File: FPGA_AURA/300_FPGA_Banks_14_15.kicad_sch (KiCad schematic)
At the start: 1 part, among them U1 XC7A35T-2FTG256C

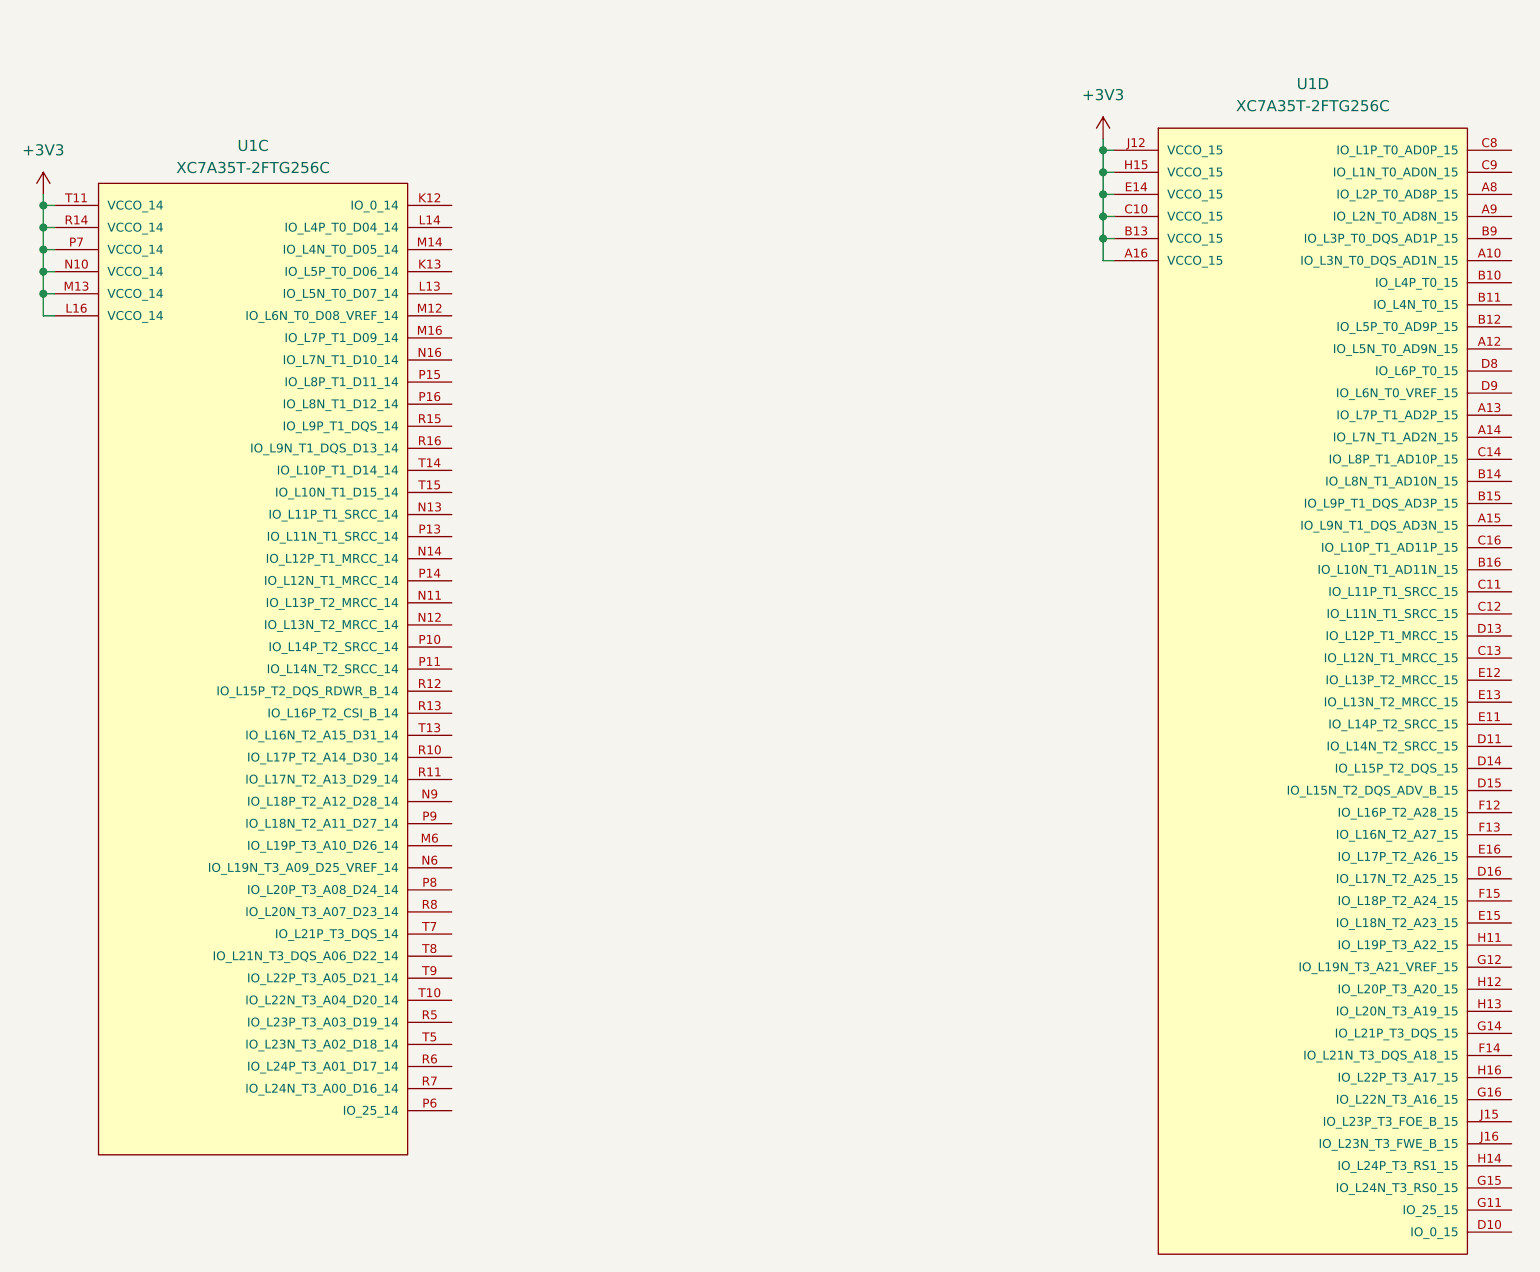
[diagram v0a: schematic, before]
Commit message: Added USB power schottky and started DDR3L
Transferring from laptop to PC to decide DDR3 pins.
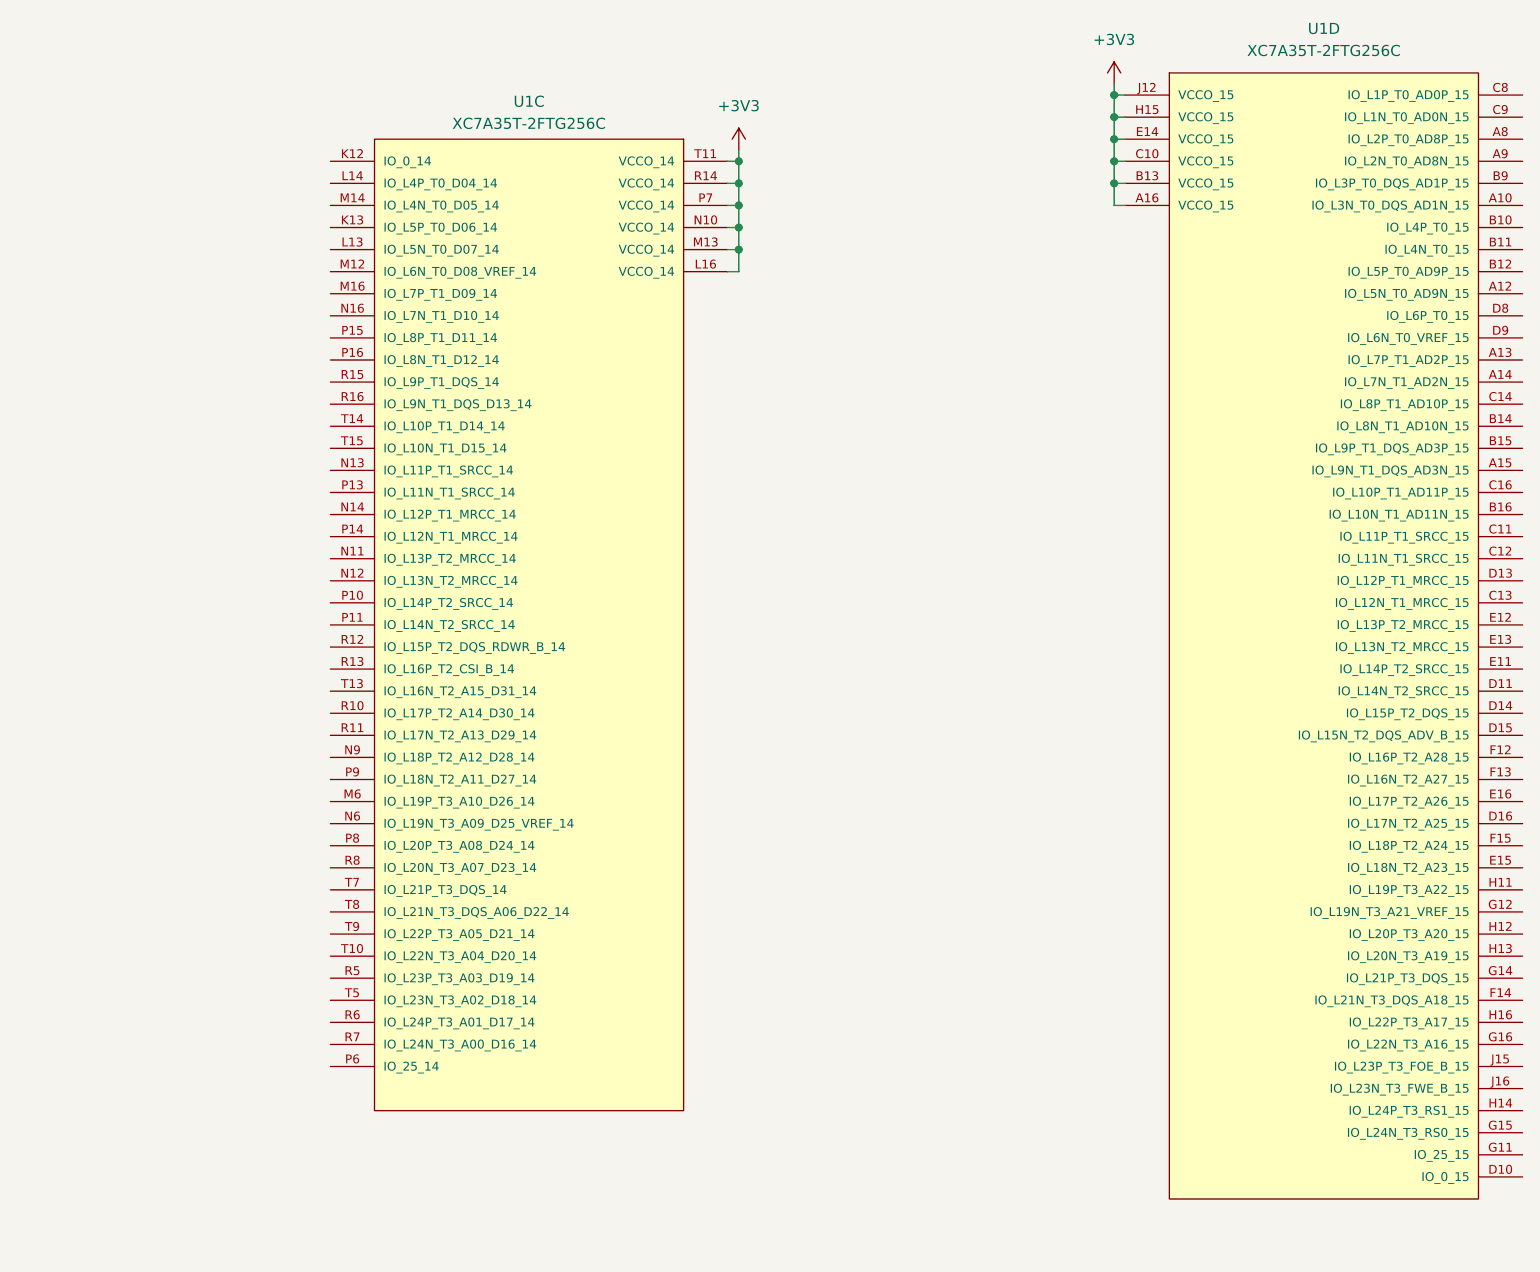
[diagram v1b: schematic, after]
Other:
- moved on the sheet: U1C, U1D

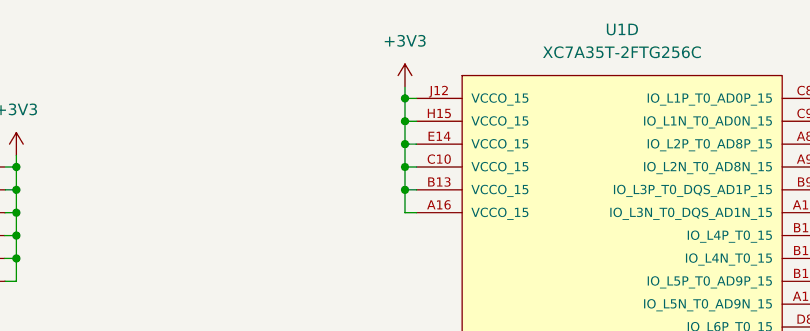
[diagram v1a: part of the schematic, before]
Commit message: Moving to PC.
Placed the VTT termination resistors roughly, rotated the DDR IC 180, and deleted the initial draft of routing.
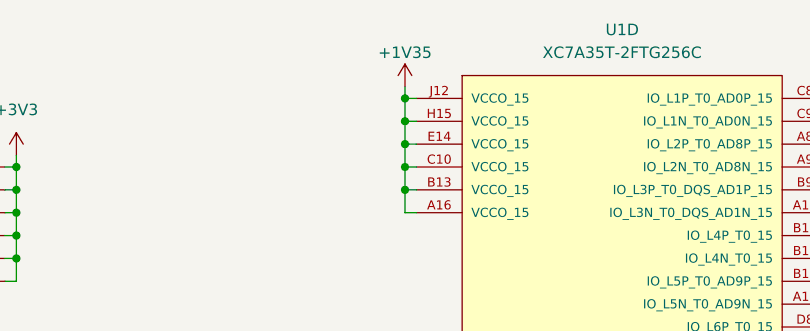
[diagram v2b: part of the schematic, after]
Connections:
- net +3V3: no longer U1.A16 (VCCO_15), U1.B13 (VCCO_15), U1.C10 (VCCO_15), U1.E14 (VCCO_15), U1.H15 (VCCO_15), U1.J12 (VCCO_15)
- new net +1V35: U1.A16 (VCCO_15), U1.B13 (VCCO_15), U1.C10 (VCCO_15), U1.E14 (VCCO_15), U1.H15 (VCCO_15), U1.J12 (VCCO_15)
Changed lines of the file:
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@@
 		(on_board yes)
 		(dnp no)
-		(fields_autoplaced yes)
 		(property "Reference" "#PWR019"
 			(at 173.99 31.75 0)
@@
 			)
 		)
-		(property "Value" "+3V3"
-			(at 173.99 22.86 0)
+		(property "Value" "+1V35"
+			(at 173.99 24.13 0)
 			(effects
 				(font
